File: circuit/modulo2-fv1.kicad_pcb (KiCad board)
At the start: 2 copper layers, 105 x 47 mm, 71 parts, among them J1 CONN_01X04, J3 CONN_01X02, J4 HOLE, J5 HOLE, J6 USB_OTG, SW1 ROTENC_BOURNS_PEL12D, U1 NE5532, U10 TLE2426, U2 PWR_CONN, U3 FV-1, U4 AVR-ISP6, U5 LM1117 3V3, U6 ATmega328p, U7 DBG_UART, U8 74164, U9 AMPCTRL, Y1 16MHz

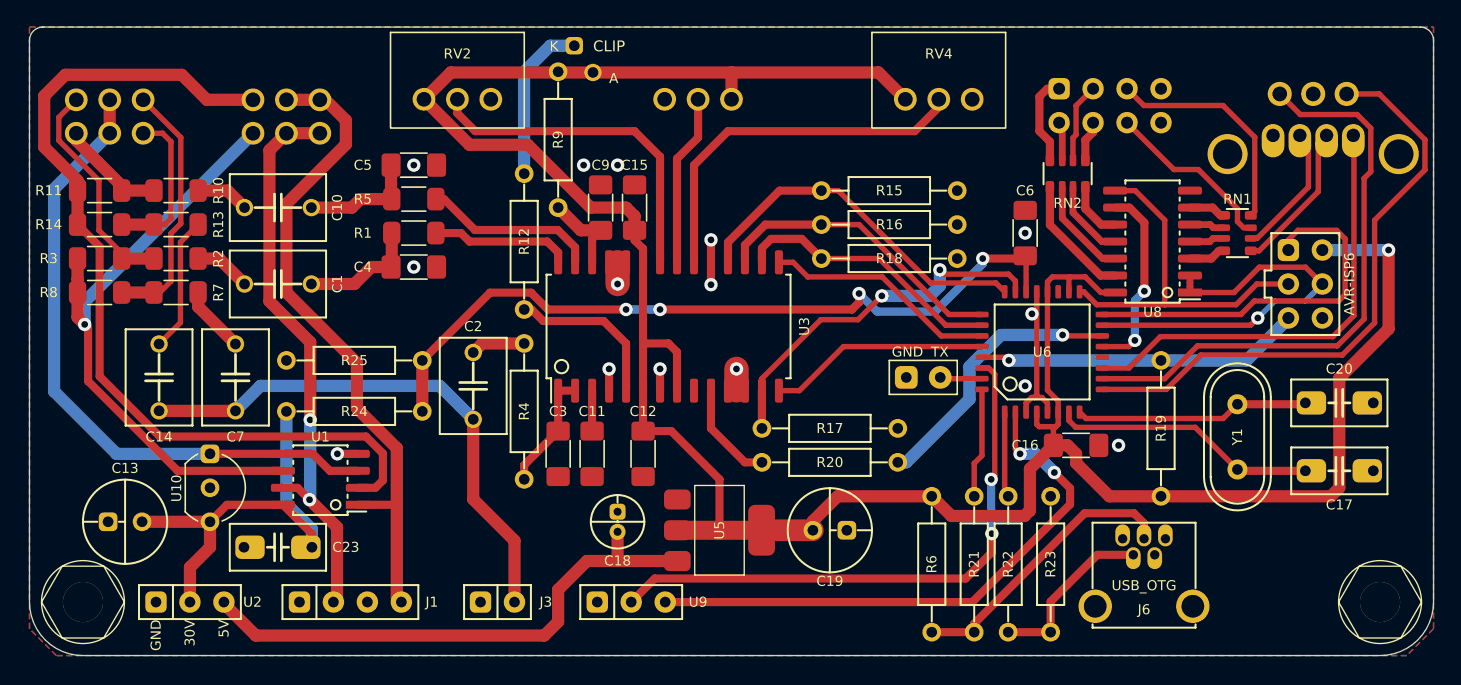
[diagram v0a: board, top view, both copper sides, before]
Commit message: ditched the LED array board; LEDs are on the main PCB now
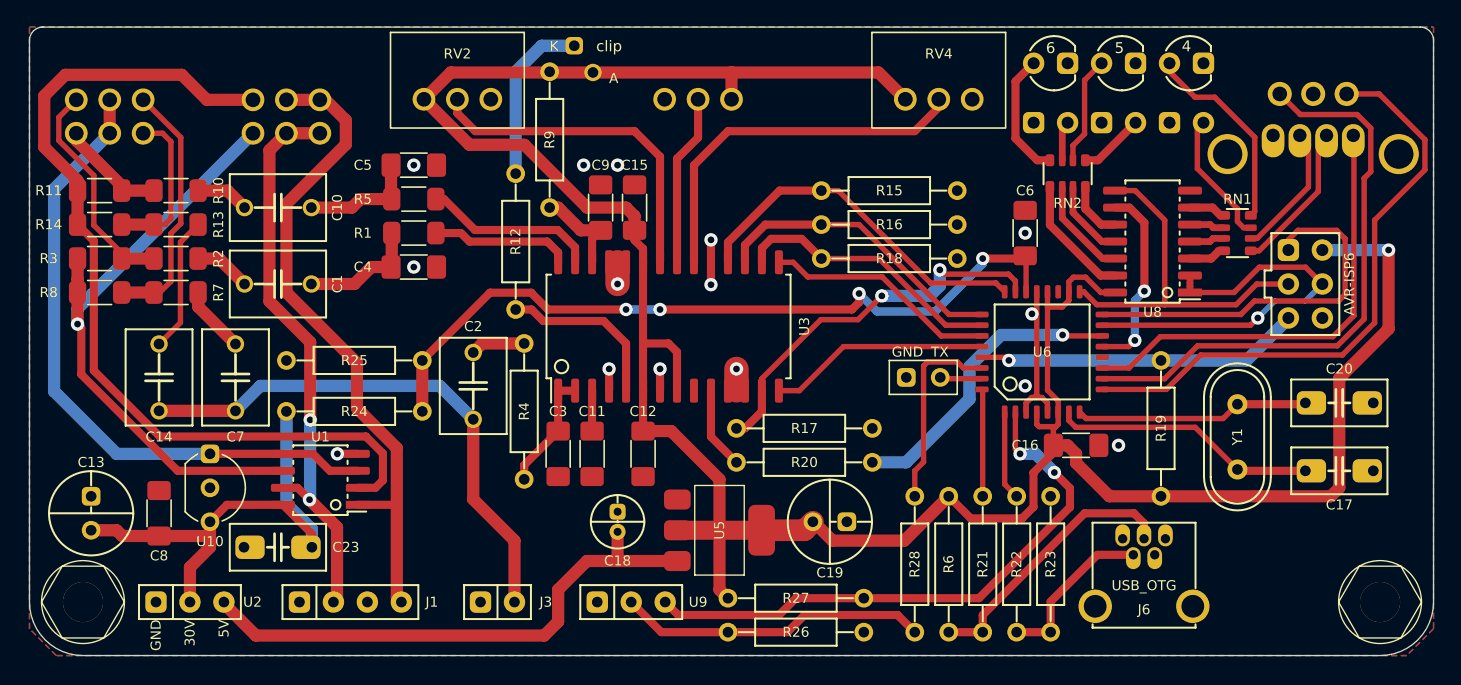
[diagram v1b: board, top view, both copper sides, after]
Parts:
- removed LA1: LED_ARRAY, myAmp:LED_ARRAY
- added C8: 100nF, myAmp:C_1206, F.Cu at (59.7, 86.4)
- added D2: 1, myAmp:LED_D3.0mm_Horizontal_Long, B.Cu at (136.5, 57.1)
- added D3: 2, myAmp:LED_D3.0mm_Horizontal_Long, B.Cu at (131.4, 57.1)
- added D4: 3, myAmp:LED_D3.0mm_Horizontal_Long, B.Cu at (126.4, 57.1)
- added D5: 4, myAmp:LED_D3.0mm_Horizontal_Short, F.Cu at (136.5, 52.7)
- added D6: 5, myAmp:LED_D3.0mm_Horizontal_Short, F.Cu at (131.4, 52.7)
- added D7: 6, myAmp:LED_D3.0mm_Horizontal_Short, F.Cu at (126.4, 52.7)
- added R26: 10K, myAmp:R_10MM, F.Cu at (107.3, 95.2)
- added R27: 10K, myAmp:R_10MM, F.Cu at (107.3, 92.7)
- added R28: 100, myAmp:R_10MM, F.Cu at (116.2, 90.2)
- C13: value 10uF -> 10µF
- D1: value CLIP -> clip
- Y1: value 16MHz -> 12MHz
- moved C13 2.62 mm to (54.6, 86.4), turned to 90 degrees
- moved R17 1.91 mm to (108.0, 80.0)
- moved R20 1.91 mm to (108.0, 82.5)
- moved R6 1.27 mm to (118.7, 90.2)
- moved R12 0.64 mm to (86.4, 66.0)
- moved R22 0.64 mm to (123.8, 90.2)
- moved C19 0.63 mm to (109.9, 87.0)
- moved R21 0.63 mm to (121.3, 90.2)
- moved R9 0.63 mm to (88.9, 58.4)
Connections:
- U9 pad 2: /POW_RST -> Net-(R26-Pad1)
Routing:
- net /POW_RST: track 43.1 -> 14.7 mm, vias 2 -> 0
- net Net-(R26-Pad1): track 0.00 -> 23.2 mm
- net +3V3: track 196.1 -> 202.2 mm
- net +24V: track 32.7 -> 36.8 mm
- net Net-(D2-Pad2): track 13.1 -> 10.0 mm
- net Net-(D7-Pad2): track 6.81 -> 9.44 mm
- net Net-(D6-Pad2): track 5.97 -> 8.14 mm
- net Net-(D5-Pad2): track 17.0 -> 15.0 mm
- net /FV_CLK: track 20.7 -> 22.6 mm
- net Net-(D3-Pad2): track 3.05 -> 4.92 mm
- net Net-(R20-Pad1): track 7.68 -> 6.15 mm
- net /T0: track 27.9 -> 29.1 mm
- net /POW_MUTE: track 42.6 -> 43.5 mm
- net Net-(J6-Pad3): track 21.4 -> 20.5 mm
- net Net-(R12-Pad2): track 12.2 -> 12.8 mm
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
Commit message: tweaked program selector LEDs
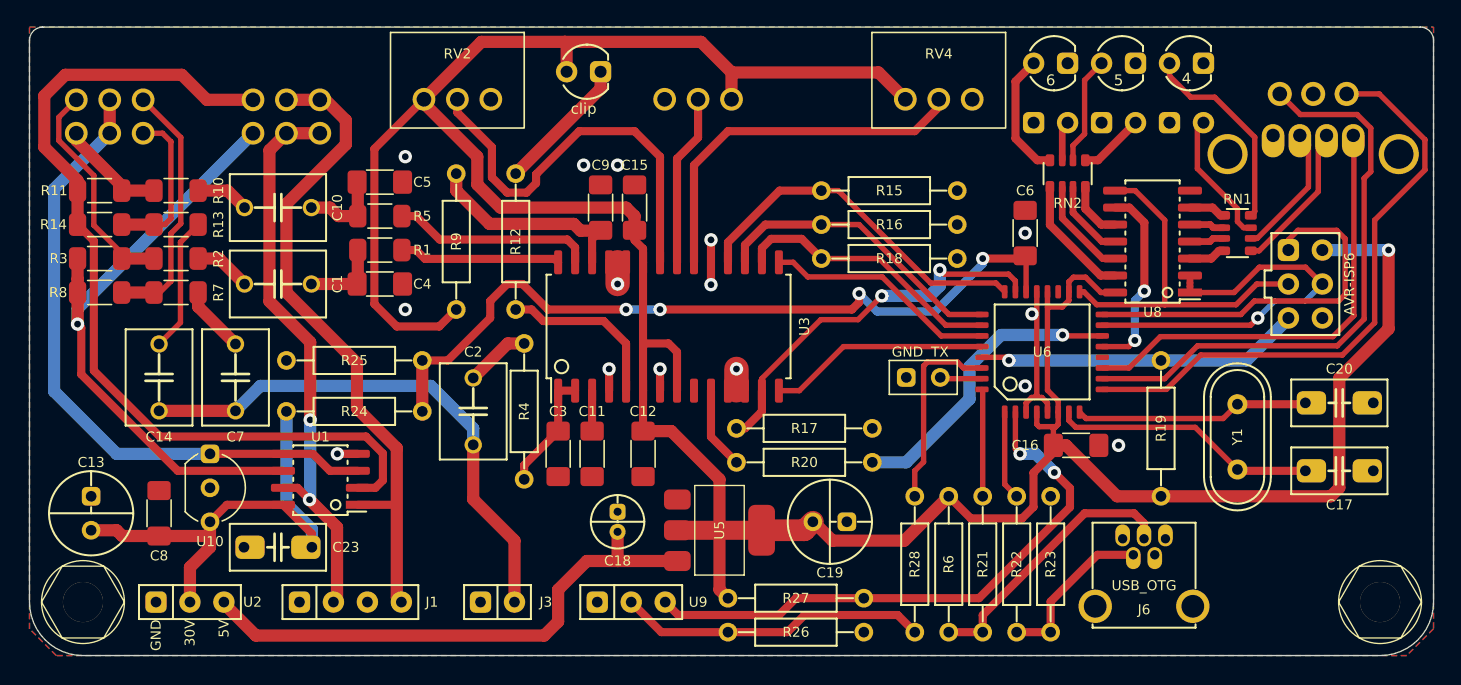
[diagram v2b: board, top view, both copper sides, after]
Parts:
- D1: footprint myAmp:LED_D3.0mm_PCBedge -> myAmp:LED_D3.0mm_Horizontal_Short
- moved R9 10.3 mm to (81.9, 66.0), turned to 90 degrees
- moved D1 2.95 mm to (91.4, 53.3), turned to 0 degrees
- moved C4 2.84 mm to (76.2, 69.2)
- moved R5 2.84 mm to (76.2, 64.1)
- moved C5 2.84 mm to (76.2, 61.6)
- moved R1 2.84 mm to (76.2, 66.7)
- moved C2 1.91 mm to (83.2, 78.7)
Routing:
- net +3V3: track 202.2 -> 231.2 mm
- net /REFP: track 7.17 -> 16.0 mm
- net Net-(RV2-Pad2): track 25.4 -> 30.9 mm
- net /FVL: track 9.05 -> 5.98 mm
- net Net-(D1-Pad1): track 12.8 -> 10.3 mm
- net /FVR: track 8.83 -> 6.29 mm
- net Net-(R5-Pad2): track 13.0 -> 15.0 mm
- net Net-(R1-Pad2): track 10.5 -> 12.1 mm
- net /IN_V: track 57.6 -> 58.9 mm
- net Net-(C2-Pad1): track 4.09 -> 4.88 mm

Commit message: almost there...
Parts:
- added T1: B0, myAmp:TestPin, F.Cu at (131.7, 78.2)
- added T2: ADC6, myAmp:TestPin, F.Cu at (126.7, 67.6)
- D1: moved to B.Cu
- moved RV5 3.59 mm to (71.8, 55.4)
- moved C17 2.62 mm to (145.4, 82.5)
- moved C20 2.62 mm to (145.4, 78.7)
- moved RV1 2.54 mm to (56.0, 55.4)
- moved D1 2.01 mm to (89.5, 52.7), turned to 180 degrees
- moved Y1 1.91 mm to (138.4, 80.6)
- moved C5 1.27 mm to (76.2, 62.9)
- moved C4 1.27 mm to (76.2, 70.5)
- moved R1 1.27 mm to (76.2, 67.9)
- moved R5 1.27 mm to (76.2, 65.4)
- moved R19 0.63 mm to (134.0, 80.0)
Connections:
- U6 pad 12: unconnected-(U6-Pad12) -> Net-(T1-Pad1)
- U6 pad 19: unconnected-(U6-Pad19) -> Net-(T2-Pad1)
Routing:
- net Net-(T1-Pad1): track 0.00 -> 6.88 mm
- net Net-(R3-Pad2): track 46.6 -> 49.1 mm
- net Net-(R11-Pad2): track 67.4 -> 70.0 mm
- net Net-(C17-Pad1): track 19.9 -> 17.5 mm
- net Net-(T2-Pad1): track 0.00 -> 2.31 mm
- net /OUTR: track 49.4 -> 51.5 mm
- net Net-(C20-Pad1): track 17.6 -> 16.0 mm
- net Net-(RV2-Pad2): track 30.9 -> 29.5 mm
- net Net-(D1-Pad1): track 10.3 -> 9.04 mm
- net +3V3: track 231.2 -> 230.1 mm
- net /OUTL: track 42.7 -> 43.7 mm
- net Net-(R5-Pad2): track 15.0 -> 14.5 mm
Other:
- board text added: "2022/03/06"
- board text added: "GND"
- board text added: "IN"
- board text added: "LFT"
- board text added: "MUT"
- board text added: "RGT"
- board text added: "RST"
- board text added: "modulo2-fv1"

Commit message: sent to fab!
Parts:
- J6: footprint myAmp:USB_OTG_THT_simple -> myAmp:USB_OTG_THT
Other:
- board text added: "2022/2/27"
- board text added: "dry/wet"
- board text added: "master"
- board text added: "par1"
- board text added: "par2"
- board text added: "par3"
- board text added: "prog"
- board text removed: "2022/03/06"
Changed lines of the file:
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@@
     (pad_to_mask_clearance 0)
     (pcbplotparams
-      (layerselection 0x0000000_7fffffff)
+      (layerselection 0x00010f0_ffffffff)
       (disableapertmacros false)
-      (usegerberextensions false)
+      (usegerberextensions true)
       (usegerberattributes true)
       (usegerberadvancedattributes true)
@@
       (sketchpadsonfab false)
       (subtractmaskfromsilk false)
-      (outputformat 5)
+      (outputformat 1)
       (mirror false)
       (drillshape 0)
       (scaleselection 1)
-      (outputdirectory "")
+      (outputdirectory "gerber/.")
     )
   )
@@
     )
   )
-  (footprint "myAmp:USB_OTG_THT_simple" (layer "F.Cu")
+  (footprint "myAmp:USB_OTG_THT" (layer "F.Cu")
     (at 133.35 88.265 90)
     (property "Sheetfile" "modulo2-fv1.kicad_sch")
@@
     (attr through_hole)
     (fp_text reference "J6" (at -5.3 0 180) (layer "F.SilkS")
-      (effects (font (size 0.75 0.75) (thickness 0.15)))
+      (effects (font (size 1 1) (thickness 0.15)))
     )
     (fp_text value "USB_OTG" (at -3.5 0 180) (layer "F.SilkS")
       (effects (font (size 0.75 0.75) (thickness 0.15)))
     )
+    (fp_line (start 1.2 -3.85) (end 1.2 3.85) (layer "F.SilkS") (width 0.15))
     (fp_line (start -6.65 -3.85) (end -6.65 3.85) (layer "F.SilkS") (width 0.15))
     (fp_line (start 1.2 3.85) (end -3.7 3.85) (layer "F.SilkS") (width 0.15))
-    (fp_line (start -6.65 3.85) (end -6.4 3.85) (layer "F.SilkS") (width 0.15))
     (fp_line (start -3.7 -3.85) (end 1.2 -3.85) (layer "F.SilkS") (width 0.15))
+    (fp_line (start -6.65 3.85) (end -6.4 3.85) (layer "F.SilkS") (width 0.15))
     (fp_line (start -6.65 -3.85) (end -6.4 -3.85) (layer "F.SilkS") (width 0.15))
-    (fp_line (start 1.2 -3.85) (end 1.2 3.85) (layer "F.SilkS") (width 0.15))
+    (fp_line (start -8.85 3.85) (end -6.65 3.85) (layer "Dwgs.User") (width 0.1524))
     (fp_line (start -8.85 -3.85) (end -6.65 -3.85) (layer "Dwgs.User") (width 0.1524))
     (fp_line (start -8.85 -3.85) (end -8.85 3.85) (layer "Dwgs.User") (width 0.1524))
-    (fp_line (start -8.85 3.85) (end -6.65 3.85) (layer "Dwgs.User") (width 0.1524))
     (pad "1" thru_hole oval (at 0 -1.6 180) (size 1.1 1.65) (drill 0.7 (offset 0 0.25)) (layers *.Cu *.Mask)
       (net 53 "unconnected-(J6-Pad1)") (pinfunction "VBUS") (pintype "power_in+no_connect"))
@@
     (pad "5" thru_hole oval (at 0 1.6 180) (size 1.1 1.65) (drill 0.7 (offset 0 0.25)) (layers *.Cu *.Mask)
       (net 5 "GND") (pinfunction "GND") (pintype "power_in"))
-    (pad "6" thru_hole circle (at -5.05 3.65 90) (size 2.5 2.5) (drill 1.7) (layers *.Cu *.Mask)
+    (pad "6" thru_hole oval (at -5.05 3.65 90) (size 2.5 1.4) (drill oval 1.9 0.8) (layers *.Cu *.Mask)
       (net 73 "unconnected-(J6-Pad6)") (pinfunction "Shield") (pintype "passive+no_connect"))
-    (pad "7" thru_hole circle (at -5.05 -3.65 90) (size 2.5 2.5) (drill 1.7) (layers *.Cu *.Mask)
+    (pad "7" thru_hole oval (at -5.05 -3.65 90) (size 2.5 1.4) (drill oval 1.9 0.8) (layers *.Cu *.Mask)
       (net 74 "unconnected-(J6-Pad7)") (pinfunction "Shield") (pintype "passive+no_connect"))
     (model "${KIPRJMOD}/myAmp.pretty/models/usb_mini_565790519.stp"
@@
   (gr_line (start 51 50) (end 154 50) (layer "Edge.Cuts") (width 0.05))
   (gr_arc (start 54 97) (mid 51.171573 95.828427) (end 50 93) (layer "Edge.Cuts") (width 0.05))
+  (gr_text "dry/wet" (at 56.145 61.33) (layer "B.SilkS")
+    (effects (font (size 1.5 1.5) (thickness 0.3)) (justify mirror))
+  )
+  (gr_text "master" (at 71.755 61.214) (layer "B.SilkS")
+    (effects (font (size 1.5 1.5) (thickness 0.3)) (justify mirror))
+  )
+  (gr_text "prog" (at 146.05 62.738) (layer "B.SilkS")
+    (effects (font (size 1.5 1.5) (thickness 0.3)) (justify mirror))
+  )
+  (gr_text "par2" (at 100.33 58.674) (layer "B.SilkS")
+    (effects (font (size 1.5 1.5) (thickness 0.3)) (justify mirror))
+  )
+  (gr_text "par3" (at 82.042 58.674) (layer "F.SilkS")
+    (effects (font (size 1.5 1.5) (thickness 0.3)))
+  )
   (gr_text "RGT" (at 77.81 94.4 90) (layer "F.SilkS")
     (effects (font (size 0.75 0.75) (thickness 0.15)) (justify right))
   )
-  (gr_text "2022/03/06" (at 102.235 52.07) (layer "F.SilkS")
+  (gr_text "2022/2/27" (at 102.235 52.07) (layer "F.SilkS")
     (effects (font (size 2 2) (thickness 0.3)))
   )
@@
     (effects (font (size 0.75 0.75) (thickness 0.15)) (justify right))
   )
+  (gr_text "par1" (at 118.11 58.674) (layer "F.SilkS")
+    (effects (font (size 1.5 1.5) (thickness 0.3)))
+  )
   (gr_text "modulo2-fv1" (at 61.595 52.07) (layer "F.SilkS")
     (effects (font (size 2 2) (thickness 0.3)))
@@
   (via (at 97.155 75.565) (size 1) (drill 0.5) (layers "F.Cu" "B.Cu") (free) (net 5))
   (via (at 93.345 75.565) (size 1) (drill 0.5) (layers "F.Cu" "B.Cu") (free) (net 5))
-  (via (at 131.709395 82.980903) (size 1) (drill 0.5) (layers "F.Cu" "B.Cu") (free) (net 5))
+  (via (at 131.709395 81.915) (size 1) (drill 0.5) (layers "F.Cu" "B.Cu") (free) (net 5))
   (via (at 80.01 69.215) (size 1) (drill 0.5) (layers "F.Cu" "B.Cu") (free) (net 5))
   (via (at 93.98 69.215) (size 1) (drill 0.5) (layers "F.Cu" "B.Cu") (net 5))
@@
   (segment (start 126.93 69.795) (end 126.93 67.748) (width 0.4064) (layer "F.Cu") (net 77))
   (segment (start 61.085577 83.185) (end 53.8734 75.972823) (width 0.6096) (layer "F.Cu") (net 78))
-  (segment (start 53.595 68.835) (end 53.595 69.85) (width 0.9144) (layer "F.Cu") (net 78))
+  (segment (start 53.595 67.31) (end 53.595 72.2112) (width 0.9144) (layer "F.Cu") (net 78))
   (segment (start 53.8734 75.972823) (end 53.8734 72.4916) (width 0.6096) (layer "F.Cu") (net 78))
   (segment (start 53.8734 72.4916) (end 53.594 72.2122) (width 0.6096) (layer "F.Cu") (net 78))
-  (segment (start 53.595 67.31) (end 53.595 68.835) (width 0.9144) (layer "F.Cu") (net 78))
-  (segment (start 53.595 69.85) (end 53.595 72.2112) (width 0.9144) (layer "F.Cu") (net 78))
   (segment (start 68.955 83.185) (end 61.085577 83.185) (width 0.6096) (layer "F.Cu") (net 78))
   (segment (start 53.595 72.2112) (end 53.594 72.2122) (width 0.9144) (layer "F.Cu") (net 78))

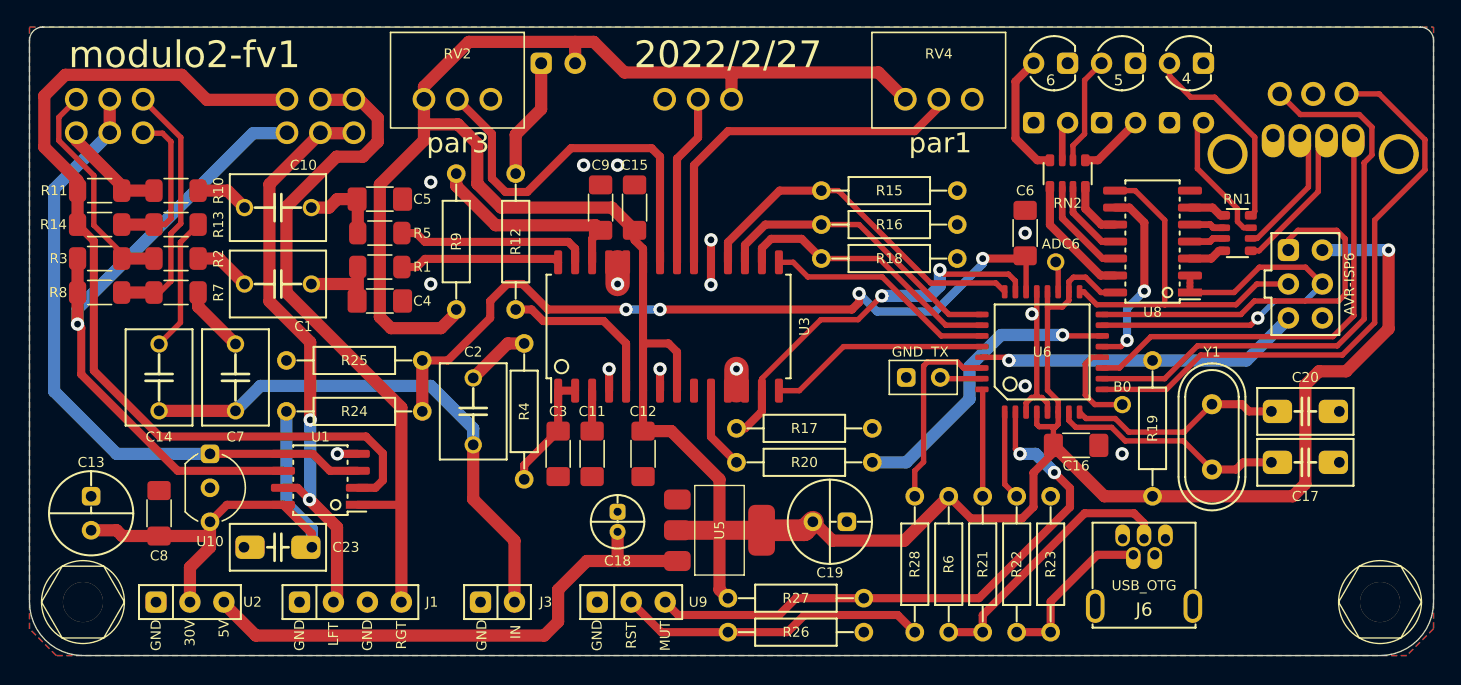
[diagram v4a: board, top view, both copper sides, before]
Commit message: fixed mistakes from assembly; added bootloader; firmware changed for PCB
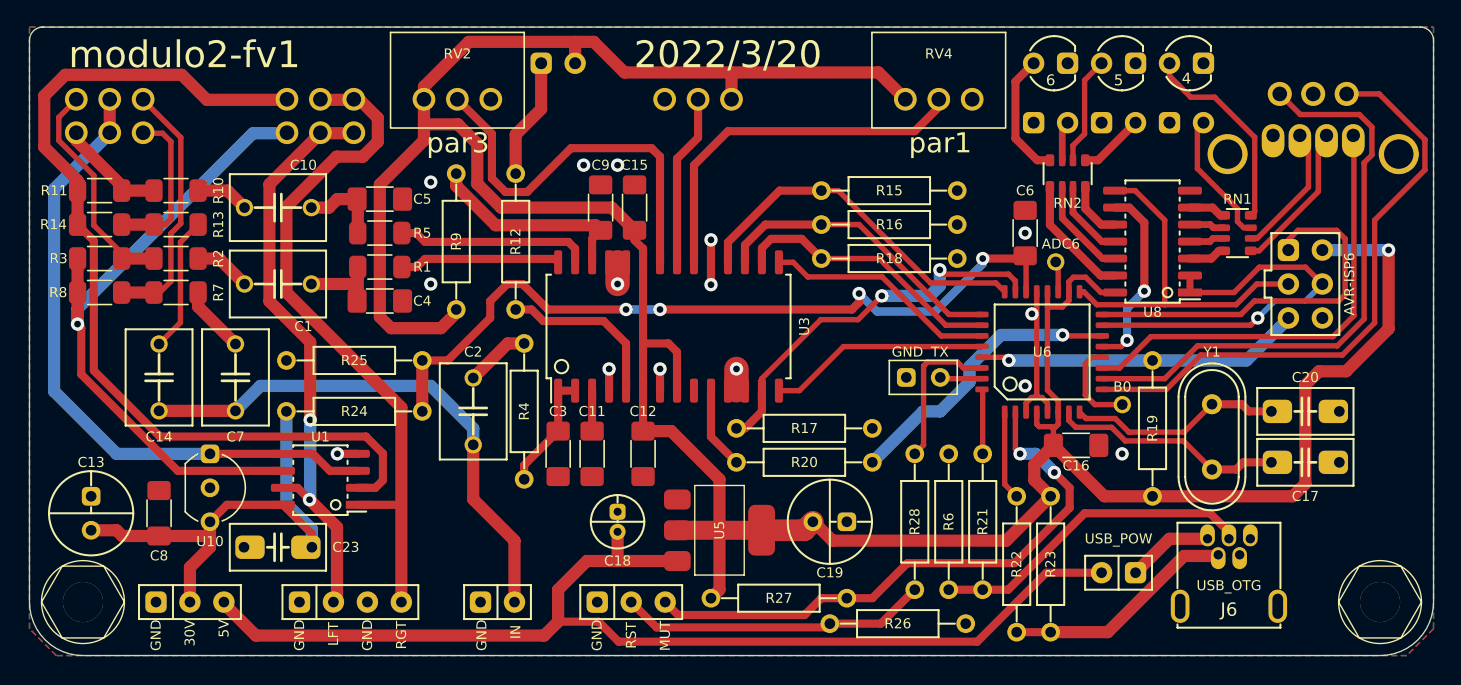
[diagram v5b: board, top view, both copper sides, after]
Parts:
- added SW2: USB_POW, myAmp:PIN_1x02, F.Cu at (131.4, 90.8)
- moved R26 7.65 mm to (114.9, 94.6)
- moved J6 6.35 mm to (139.7, 88.3)
- moved R21 3.17 mm to (121.3, 87.0)
- moved R28 3.17 mm to (116.2, 87.0)
- moved R6 3.17 mm to (118.7, 87.0)
- moved R27 1.27 mm to (106.0, 92.7)
- turned R23 to 90 degrees
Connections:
- J6 pad 1: unconnected-(J6-Pad1) -> Net-(J6-Pad1)
- R23 pad 1: GND -> Net-(J6-Pad2)
- R23 pad 2: Net-(J6-Pad2) -> +3V3
- R6 pad 2: +3V3 -> GND
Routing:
- net +5V: track 40.9 -> 84.3 mm
- net Net-(J6-Pad1): track 0.00 -> 6.44 mm
- net Net-(J6-Pad2): track 12.5 -> 17.5 mm
- net Net-(J6-Pad3): track 20.5 -> 24.4 mm
- net /POW_RST: track 14.7 -> 11.5 mm
- net /D+: track 8.02 -> 4.84 mm
- net /FV_CLK: track 22.6 -> 21.8 mm
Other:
- board text added: "2022/3/20"
- board text removed: "2022/2/27"
